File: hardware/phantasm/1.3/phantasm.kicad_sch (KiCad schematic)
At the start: 30 parts, among them J1 TBC05-02-1-G-G +5V IN ~1A, J2 TBC05-03-1-G-G LED DI/SIG_GND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, J3A TBC05-04-1-G-G SYNC in, J3B TBC05-04-1-G-G SYNC out, U1 74AHCT125

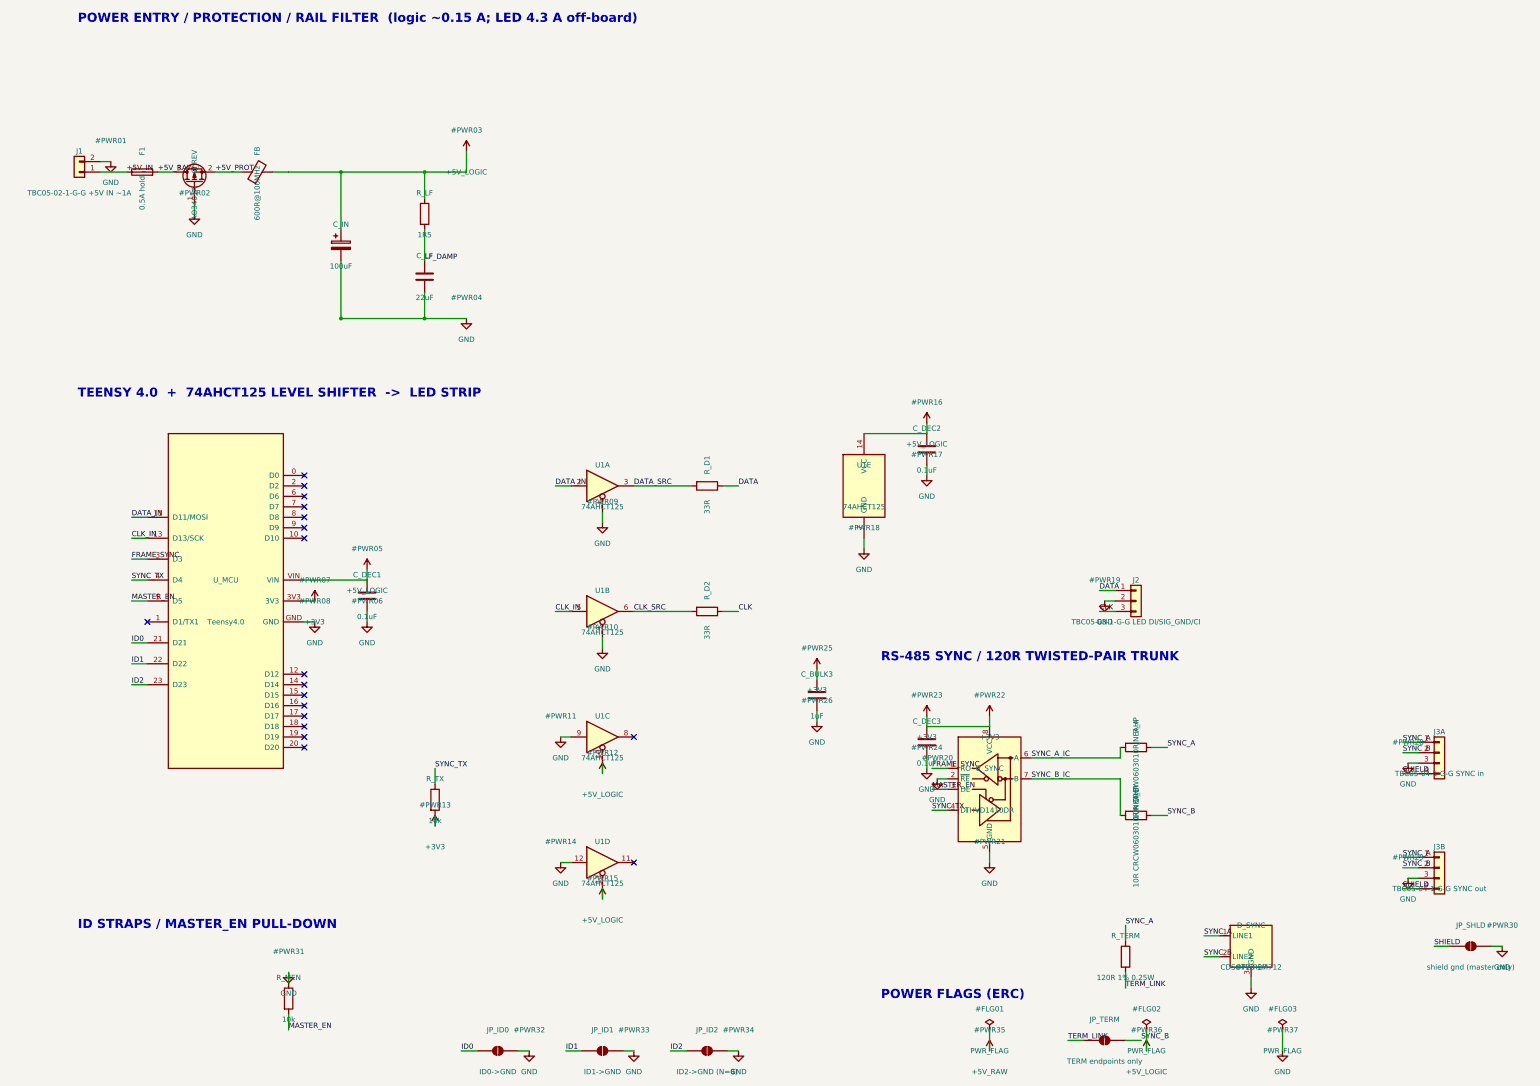
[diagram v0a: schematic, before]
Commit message: pcb: strengthen rev 1.3 differential sync and specify components
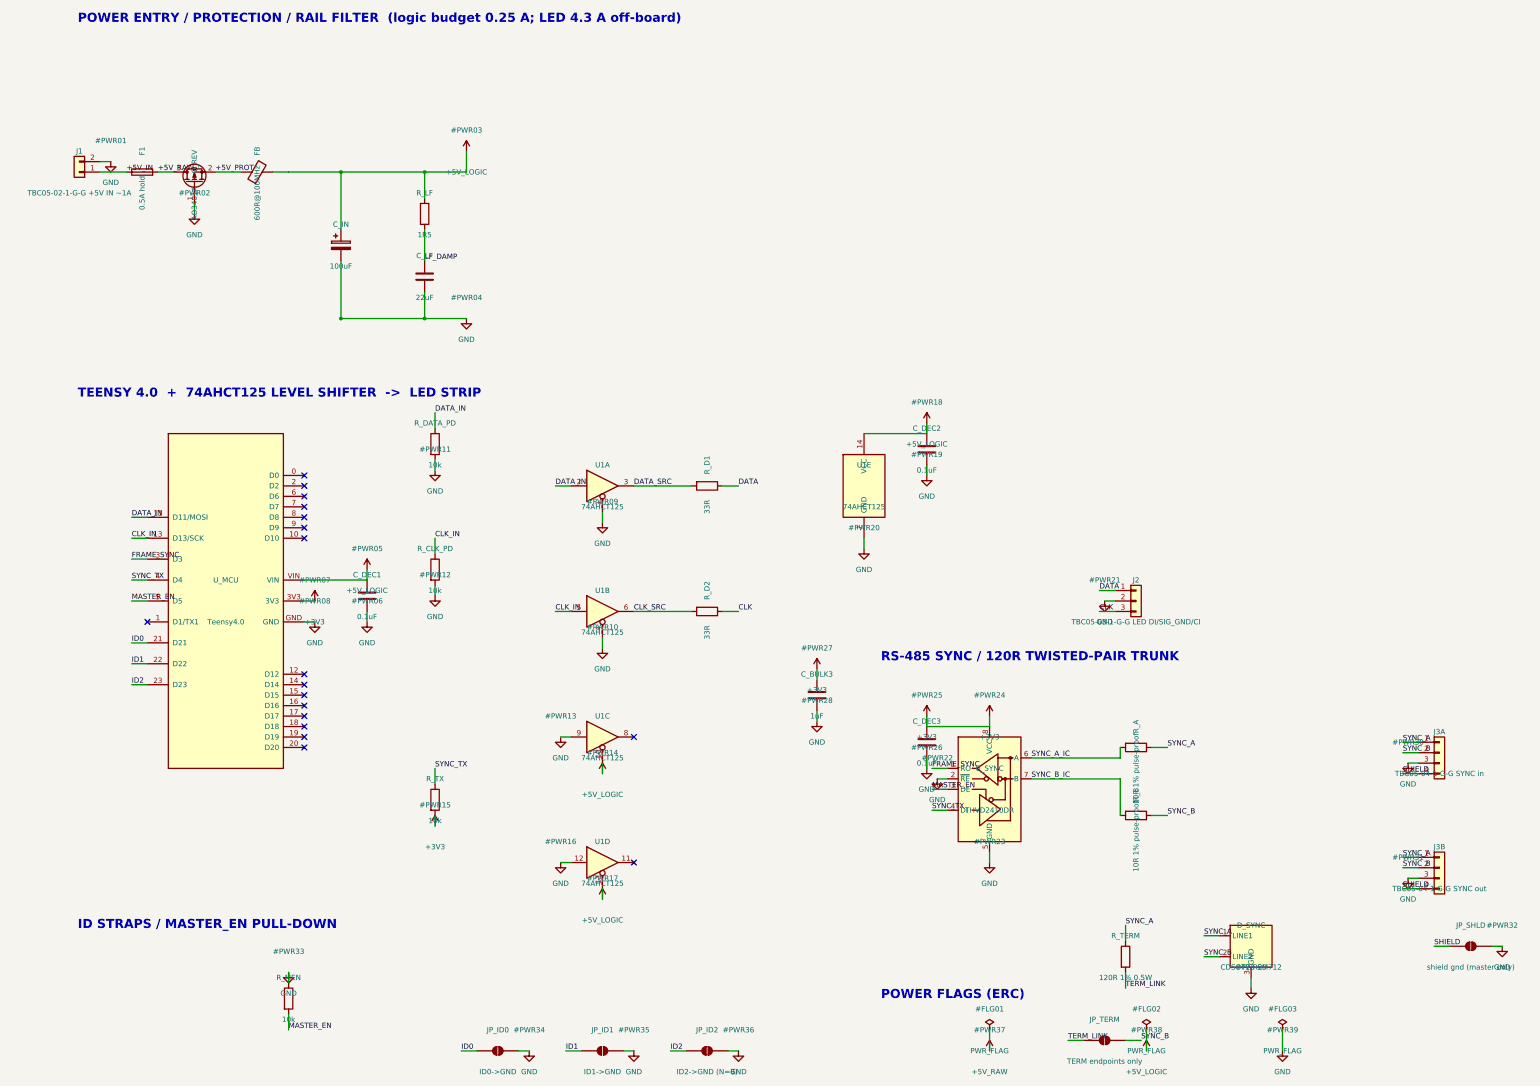
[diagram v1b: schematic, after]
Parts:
- removed C_BULK3: 1uF, Capacitor_SMD:C_0603_1608Metric, symbol Device:C
- removed D_SYNC: CDSOT23-SM712, Package_TO_SOT_SMD:SOT-23, symbol phantasm:CDSOT23-SM712
- removed R_A: 10R CRCW0603010RJNEAHP, Resistor_SMD:R_0603_1608Metric_Pad0.98x0.95mm_HandSolder, symbol Device:R
- removed U_SYNC: THVD1410DR, Package_SO:SOIC-8_3.9x4.9mm_P1.27mm, symbol phantasm:THVD1410DR
- added C_DEC3: 0.1uF, Capacitor_SMD:C_0603_1608Metric, symbol Device:C
- added J2: TBC05-03-1-G-G LED DI/SIG_GND/CI, phantasm:TerminalBlock_GCT_TBC05-03-1-G-G, symbol Connector_Generic:Conn_01x03
- added JP_ID1: ID1->GND, Jumper:SolderJumper-2_P1.3mm_Open_RoundedPad1.0x1.5mm, symbol Jumper:SolderJumper_2_Open
- added JP_ID2: ID2->GND (N=8), Jumper:SolderJumper-2_P1.3mm_Open_RoundedPad1.0x1.5mm, symbol Jumper:SolderJumper_2_Open
- added R_B: 10R 1% pulse-proof, Resistor_SMD:R_0603_1608Metric_Pad0.98x0.95mm_HandSolder, symbol Device:R
- added R_DATA_PD: 10k, Resistor_SMD:R_0603_1608Metric, symbol Device:R
- C_BULK3: renamed from R_B; value 10R CRCW0603010RJNEAHP -> 1uF; footprint Resistor_SMD:R_0603_1608Metric_Pad0.98x0.95mm_HandSolder -> Capacitor_SMD:C_0603_1608Metric; symbol Device:R -> Device:C; MPN (none) -> CC0603KRX7R8BB105; Manufacturer (none) -> YAGEO
- C_DEC1: MPN (none) -> CC0603KRX7R9BB104; Manufacturer (none) -> YAGEO
- C_DEC2: renamed from J2; value TBC05-03-1-G-G LED DI/SIG_GND/CI -> 0.1uF; footprint phantasm:TerminalBlock_GCT_TBC05-03-1-G-G -> Capacitor_SMD:C_0603_1608Metric; symbol Connector_Generic:Conn_01x03 -> Device:C; MPN (none) -> CC0603KRX7R9BB104; Manufacturer (none) -> YAGEO; now in the parts list
- C_IN: MPN (none) -> UPW1H101MPD; Manufacturer (none) -> Nichicon
- D_SYNC: renamed from J3B; value TBC05-04-1-G-G SYNC out -> CDSOT23-SM712; footprint phantasm:TerminalBlock_GCT_TBC05-04-1-G-G -> Package_TO_SOT_SMD:SOT-23; symbol Connector_Generic:Conn_01x04 -> phantasm:CDSOT23-SM712; MPN (none) -> CDSOT23-SM712; Manufacturer (none) -> Bourns; now in the parts list
- J3A: renamed from R_TERM; value 120R 1% 0.25W -> TBC05-04-1-G-G SYNC in; footprint Resistor_SMD:R_0805_2012Metric_Pad1.20x1.40mm_HandSolder -> phantasm:TerminalBlock_GCT_TBC05-04-1-G-G; symbol Device:R -> Connector_Generic:Conn_01x04; now left out of the parts list
- J3B: renamed from JP_SHLD; value shield gnd (master only) -> TBC05-04-1-G-G SYNC out; footprint Jumper:SolderJumper-2_P1.3mm_Open_RoundedPad1.0x1.5mm -> phantasm:TerminalBlock_GCT_TBC05-04-1-G-G; symbol Jumper:SolderJumper_2_Open -> Connector_Generic:Conn_01x04
- JP_ID0: renamed from JP_ID2; value ID2->GND (N=8) -> ID0->GND
- JP_SHLD: renamed from JP_ID0; value ID0->GND -> shield gnd (master only)
- R_A: renamed from J3A; value TBC05-04-1-G-G SYNC in -> 10R 1% pulse-proof; footprint phantasm:TerminalBlock_GCT_TBC05-04-1-G-G -> Resistor_SMD:R_0603_1608Metric_Pad0.98x0.95mm_HandSolder; symbol Connector_Generic:Conn_01x04 -> Device:R; MPN (none) -> CRCW060310R0FKEAHP; Manufacturer (none) -> Vishay; now in the parts list
- R_CLK_PD: renamed from R_TX; MPN (none) -> RC0603FR-0710KL; Manufacturer (none) -> YAGEO
- R_MEN: renamed from JP_ID1; value ID1->GND -> 10k; footprint Jumper:SolderJumper-2_P1.3mm_Open_RoundedPad1.0x1.5mm -> Resistor_SMD:R_0603_1608Metric; symbol Jumper:SolderJumper_2_Open -> Device:R; MPN (none) -> RC0603FR-0710KL; Manufacturer (none) -> YAGEO; now in the parts list
- R_TERM: renamed from R_MEN; value 10k -> 120R 1% 0.5W; footprint Resistor_SMD:R_0603_1608Metric -> Resistor_SMD:R_0805_2012Metric_Pad1.20x1.40mm_HandSolder; MPN (none) -> CRCW0805120RFKEAHP; Manufacturer (none) -> Vishay
- R_TX: renamed from C_DEC2; value 0.1uF -> 10k; footprint Capacitor_SMD:C_0603_1608Metric -> Resistor_SMD:R_0603_1608Metric; symbol Device:C -> Device:R; MPN (none) -> RC0603FR-0710KL; Manufacturer (none) -> YAGEO
- U_SYNC: renamed from C_DEC3; value 0.1uF -> THVD2410DR; footprint Capacitor_SMD:C_0603_1608Metric -> Package_SO:SOIC-8_3.9x4.9mm_P1.27mm; symbol Device:C -> phantasm:THVD2410DR; MPN (none) -> THVD2410DR; Manufacturer (none) -> Texas Instruments
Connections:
- net +3V3: now also C_BULK3.1, R_TX.2, U_SYNC.8 (VCC), C_DEC3.1; no longer R_CLK_PD.2, U_SYNC.1
- net +5V_LOGIC: now also C_DEC2.1; no longer R_TX.1
- net CLK: now also J2.3 (Pin_3); no longer C_DEC2.3 (Pin_3)
- net CLK_IN: now also R_CLK_PD.1
- net DATA: now also J2.1 (Pin_1); no longer C_DEC2.1 (Pin_1)
- net DATA_IN: now also R_DATA_PD.1
- net FRAME_SYNC: now also U_SYNC.1 (RO)
- net GND: now also C_BULK3.2, J3A.3 (Pin_3), J3B.3 (Pin_3), R_CLK_PD.2, R_MEN.1, U_SYNC.5 (GND), C_DEC3.2, J2.2 (Pin_2), JP_ID1.2 (B), JP_ID2.2 (B), R_DATA_PD.2; no longer J3B.2 (B), R_A.3 (Pin_3), R_MEN.2 (B), R_TERM.1, R_TX.2
- net ID0: now also JP_ID0.1 (A); no longer JP_SHLD.1 (A)
- net ID1: now also JP_ID1.1 (A); no longer R_MEN.1 (A)
- net ID2: now also JP_ID2.1 (A); no longer JP_ID0.1 (A)
- net MASTER_EN: now also R_MEN.2, U_SYNC.3 (DE); no longer R_TERM.2
- net SHIELD: now also J3A.4 (Pin_4), J3B.4 (Pin_4), JP_SHLD.1 (A); no longer D_SYNC.4 (Pin_4), J3B.1 (A), R_A.4 (Pin_4)
- net SYNC_A: now also J3B.1 (Pin_1), R_TERM.1
- net SYNC_A_IC: now also R_A.2, U_SYNC.6 (A)
- net SYNC_B: now also J3A.2 (Pin_2), J3B.2 (Pin_2), R_B.1; no longer C_BULK3.1, R_A.2 (Pin_2)
- net SYNC_B_IC: now also U_SYNC.7 (B), R_B.2; no longer C_BULK3.2
- net SYNC_TX: now also R_TX.1, U_SYNC.4 (DI); no longer R_CLK_PD.1
- net TERM_LINK: now also R_TERM.2; no longer J3A.2
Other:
- note added: "POWER ENTRY / PROTECTION / RAIL FILTER (logic budget 0.25 A; LED 4.3 A off-board)"
- note removed: "POWER ENTRY / PROTECTION / RAIL FILTER (logic ~0.15 A; LED 4.3 A off-board)"
- moved on the sheet: JP_ID0, JP_SHLD, R_CLK_PD, R_TERM
